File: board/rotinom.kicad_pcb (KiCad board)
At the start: 2 copper layers, 109 parts, among them J1 Conn_01x04, J2 Conn_01x04, J3 Conn_01x02, J4 Styx_P4, J5 Styx_P5, P1 test_connector, Q1 MMBT2369, Q10 MMBT2369, Q11 MMBT2369, Q12 MMBT2369, Q13 MMBT2369, Q14 MMBT2369, Q15 MMBT2369, Q16 MMBT2369, Q17 MMBT2369, Q18 MMBT2369, Q19 MMBT2369, Q2 MMBT2369, Q20 MMBT2369, Q21 MMBT2369, Q22 MMBT2369, Q23 MMBT2369, Q24 MMBT2369, Q25 MMBT2369, Q26 MMBT2369, Q27 MMBT2369, Q28 MMBT2369, Q29 MMBT2369, Q3 MMBT2369, Q30 MMBT2369, Q31 MMBT2369, Q32 MMBT2369, Q33 MMBT2369, Q4 MMBT2369, Q5 MMBT2369, Q6 MMBT2369, Q7 MMBT2369, Q8 MMBT2369, Q9 MMBT2369

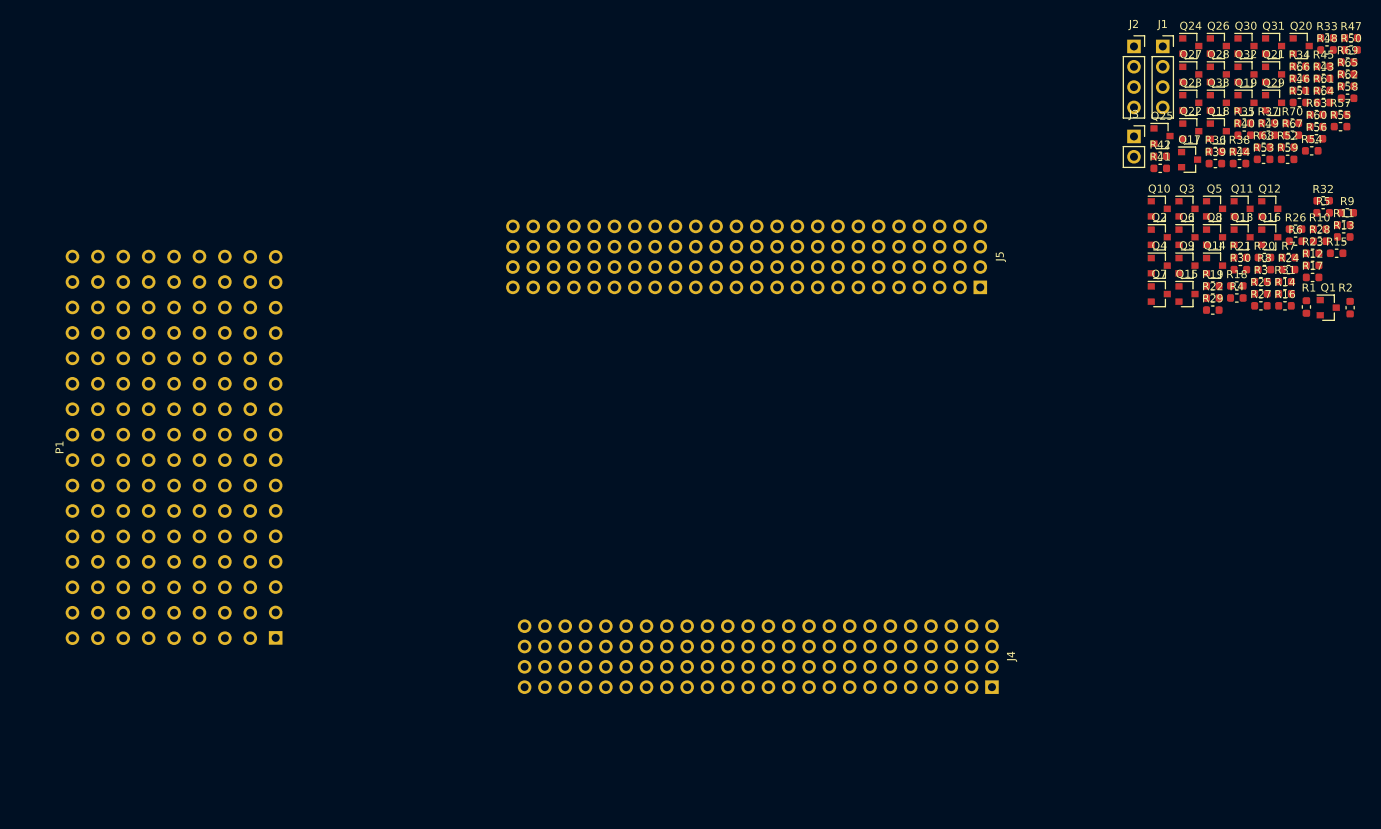
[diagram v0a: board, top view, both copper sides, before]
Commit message: Board: 5/8 of the data lanes routed
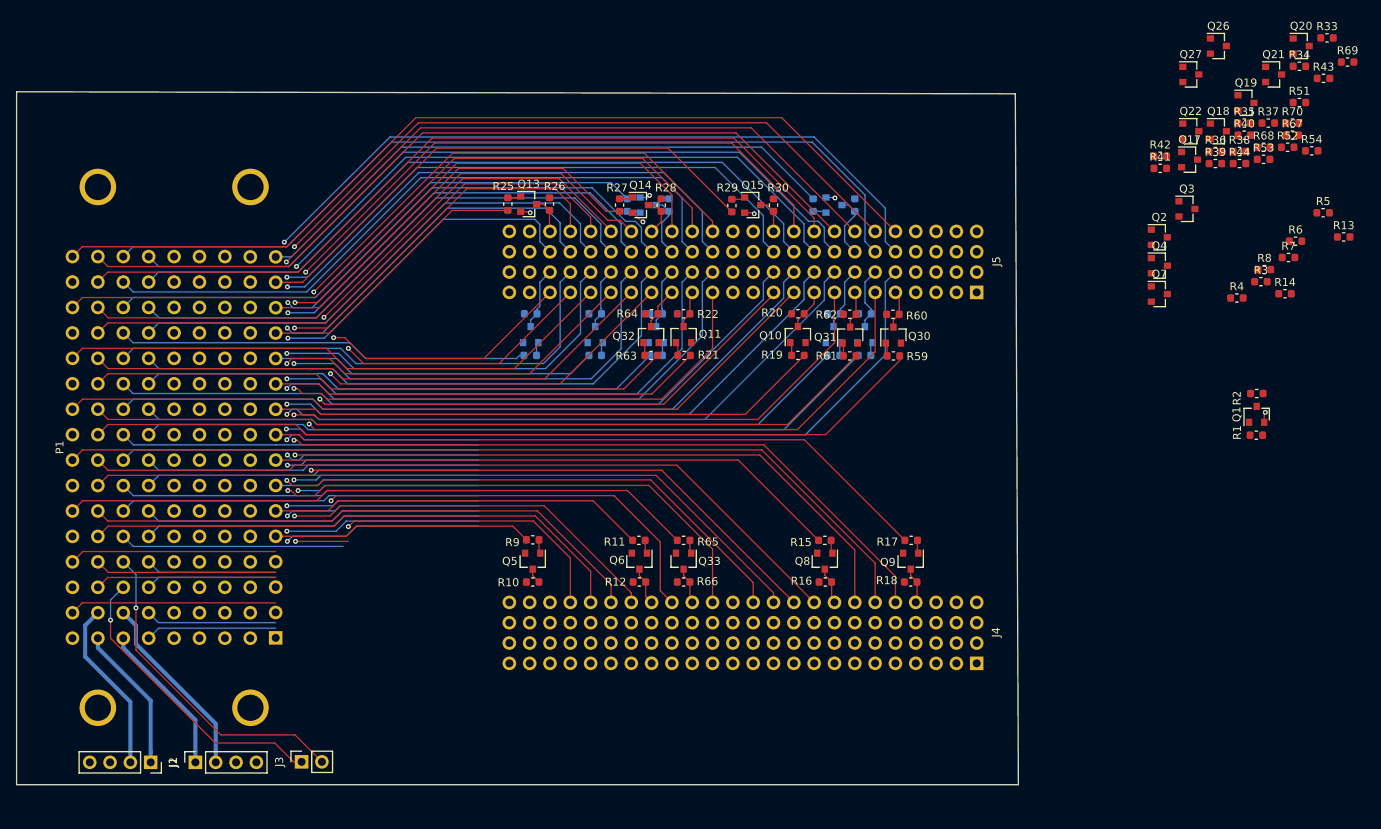
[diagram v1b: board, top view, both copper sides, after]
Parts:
- added H1: MountingHole_Pad, agc_monitor:MountingHole_ANSI_4, F.Cu at (66.7, 69.0)
- added H2: MountingHole_Pad, agc_monitor:MountingHole_ANSI_4, F.Cu at (85.8, 69.0)
- added H3: MountingHole_Pad, agc_monitor:MountingHole_ANSI_4, F.Cu at (66.7, 134.2)
- added H4: MountingHole_Pad, agc_monitor:MountingHole_ANSI_4, F.Cu at (85.8, 134.2)
- Q12, Q16, Q23, Q24, Q25, Q28, Q29, R23, R24, R31, R32, R45, R46, R47, R48, R49, R50, R55, R56, R57, R58: moved to B.Cu
- moved J1 155.0 mm to (73.3, 141.0), turned to 270 degrees
- moved J2 147.6 mm to (78.9, 141.0), turned to 90 degrees
- moved J3 130.1 mm to (92.1, 140.9), turned to 90 degrees
- moved R9 109.7 mm to (121.0, 113.2), turned to 180 degrees
- moved R10 107.8 mm to (121.0, 118.4)
- moved R55 105.3 mm to (120.7, 90.1), turned to 180 degrees
- moved R65 101.4 mm to (139.9, 113.2), turned to 180 degrees
- moved R56 100.6 mm to (120.8, 84.9)
- moved R66 99.4 mm to (139.9, 118.4)
- moved R11 96.5 mm to (134.3, 113.2), turned to 180 degrees
- moved Q5 95.9 mm to (121.0, 115.8), turned to 270 degrees
- moved R25 94.8 mm to (117.9, 71.2), turned to 270 degrees
- moved R26 93.3 mm to (123.1, 71.2), turned to 270 degrees
- moved R12 93.0 mm to (134.4, 118.4)
- moved R50 92.9 mm to (136.5, 84.9)
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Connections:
- J4 pad 16: Net-(J4-Pad16) -> MDT09_n
- J4 pad 20: Net-(J4-Pad20) -> MT09
- J4 pad 24: Net-(J4-Pad24) -> MSP908
- J4 pad 28: Net-(J4-Pad28) -> MT08
- J4 pad 32: Net-(J4-Pad32) -> MDT08_n
- J4 pad 36: Net-(J4-Pad36) -> MSCDBL_n
- J4 pad 40: Net-(J4-Pad40) -> MWL08
- J4 pad 44: Net-(J4-Pad44) -> MSP807
- J4 pad 48: Net-(J4-Pad48) -> MWL07
- J4 pad 56: Net-(J4-Pad56) -> MT07
- J4 pad 60: Net-(J4-Pad60) -> MAMU_n
- J4 pad 64: Net-(J4-Pad64) -> MT06
- J4 pad 68: Net-(J4-Pad68) -> MDT06_n
- J4 pad 72: Net-(J4-Pad72) -> MWL06
- J4 pad 76: Net-(J4-Pad76) -> MSP806
- J4 pad 80: Net-(J4-Pad80) -> MSP805
- J4 pad 84: Net-(J4-Pad84) -> MWL05
- J4 pad 88: Net-(J4-Pad88) -> MDT05_n
- J5 pad 17: Net-(J5-Pad17) -> NHALGA_n
- J5 pad 18: Net-(J5-Pad18) -> MWBG
- J5 pad 19: Net-(J5-Pad19) -> MRLG
- J5 pad 20: Net-(J5-Pad20) -> MSP916
- J5 pad 21: Net-(J5-Pad21) -> MWL09
- J5 pad 22: Net-(J5-Pad22) -> MSBSTP_n
- J5 pad 23: Net-(J5-Pad23) -> MPIPAL_n
- J5 pad 24: Net-(J5-Pad24) -> MWBBEG
- J5 pad 25: Net-(J5-Pad25) -> DOSCAL_n
- J5 pad 26: Net-(J5-Pad26) -> MRDCH_n
- J5 pad 27: Net-(J5-Pad27) -> MDT16_n
- J5 pad 28: Net-(J5-Pad28) -> MWL16
- J5 pad 29: Net-(J5-Pad29) -> MWL10
- J5 pad 30: Net-(J5-Pad30) -> MSQ10
- J5 pad 31: Net-(J5-Pad31) -> MRAG
- J5 pad 32: Net-(J5-Pad32) -> MVFAIL_n
- J5 pad 33: Net-(J5-Pad33) -> MDT10_n
- J5 pad 34: Net-(J5-Pad34) -> MGOJAM
- J5 pad 35: Net-(J5-Pad35) -> MSQ16
- J5 pad 36: Net-(J5-Pad36) -> MOSCAL_n
- J5 pad 37: Net-(J5-Pad37) -> MSP910
- J5 pad 38: Net-(J5-Pad38) -> MNISQ
- J5 pad 39: Net-(J5-Pad39) -> MWAG
- J5 pad 40: Net-(J5-Pad40) -> MWL15
- J5 pad 41: Net-(J5-Pad41) -> MT10
- J5 pad 42: Net-(J5-Pad42) -> MREQIN
- J5 pad 43: Net-(J5-Pad43) -> MSQEXT
- J5 pad 44: Net-(J5-Pad44) -> MDT15_n
- J5 pad 53: Net-(J5-Pad53) -> MT11
- J5 pad 54: Net-(J5-Pad54) -> MINHL
- J5 pad 55: Net-(J5-Pad55) -> MRSC
- J5 pad 56: Net-(J5-Pad56) -> MWEBG
- J5 pad 57: Net-(J5-Pad57) -> MDT11_n
- J5 pad 58: Net-(J5-Pad58) -> MSQ11
- J5 pad 59: Net-(J5-Pad59) -> MON800
- J5 pad 60: Net-(J5-Pad60) -> MSP914
- J5 pad 61: Net-(J5-Pad61) -> DBLTST_n
- J5 pad 62: Net-(J5-Pad62) -> MLDCH_n
- J5 pad 63: Net-(J5-Pad63) -> MREAD_n
- J5 pad 64: Net-(J5-Pad64) -> MWFBG
- J5 pad 65: Net-(J5-Pad65) -> MWL11
- J5 pad 66: Net-(J5-Pad66) -> MGP_n
- J5 pad 67: Net-(J5-Pad67) -> MONWT
- J5 pad 68: Net-(J5-Pad68) -> MDT14_n
- J5 pad 69: Net-(J5-Pad69) -> MWARNF_n
- J5 pad 70: Net-(J5-Pad70) -> MSQ12
- J5 pad 71: Net-(J5-Pad71) -> MSQ14
- J5 pad 72: Net-(J5-Pad72) -> MSCAFL_n
- J5 pad 73: Net-(J5-Pad73) -> MWL12
- J5 pad 74: Net-(J5-Pad74) -> MDT12_n
- J5 pad 75: Net-(J5-Pad75) -> MRGG
- J5 pad 76: Net-(J5-Pad76) -> MWL14
- J5 pad 77: Net-(J5-Pad77) -> MSP912
- J5 pad 78: Net-(J5-Pad78) -> MINKL
- J5 pad 79: Net-(J5-Pad79) -> MSP
- J5 pad 80: Net-(J5-Pad80) -> OUTCOM
- J5 pad 81: Net-(J5-Pad81) -> MT12
- J5 pad 82: Net-(J5-Pad82) -> MWATCH_n
- J5 pad 83: Net-(J5-Pad83) -> MSQ13
- J5 pad 84: Net-(J5-Pad84) -> MWL13
- J5 pad 85: Net-(J5-Pad85) -> MRULOG
- J5 pad 86: Net-(J5-Pad86) -> MLOAD_n
- J5 pad 87: Net-(J5-Pad87) -> MWLG
- J5 pad 88: Net-(J5-Pad88) -> MDT13_n
- R45 pad 2: MSTBSTP -> MSBSTP
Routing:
- net MSP916: track 0.00 -> 115.9 mm
- net MSP908: track 0.00 -> 111.6 mm
- net MPIPAL_n: track 0.00 -> 109.0 mm
- net NHALGA: track 0.00 -> 105.7 mm
- net MRLG: track 0.00 -> 104.7 mm, vias 0 -> 1
- net MVFAIL_n: track 0.00 -> 104.6 mm
- net MOSCAL_n: track 0.00 -> 102.8 mm
- net MWBG: track 0.00 -> 101.8 mm, vias 0 -> 1
- net DOSCAL: track 0.00 -> 99.1 mm
- net MRAG: track 0.00 -> 98.3 mm
- net MSCDBL_n: track 0.00 -> 97.4 mm
- net MSP910: track 0.00 -> 97.3 mm
- net MT09: track 0.00 -> 94.9 mm, vias 0 -> 1
- net MWBBEG: track 0.00 -> 93.8 mm, vias 0 -> 1
- net MSBSTP: track 0.00 -> 93.3 mm
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- added copper zone on In2.Cu, net GND
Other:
- board outline added: 125.2 x 86.6 mm
- copper layers 2 -> 4
- net class Default: clearance 0.2 -> 0.1524; trace_width 0.25 -> 0.1524; via_dia 0.8 -> 0.6096; via_drill 0.4 -> 0.3048
- rule trace_clearance: 0.2 -> 0.1524
- rule trace_min: 0.2 -> 0.1524
- rule via_min_drill: 0.3 -> 0.3048
- rule via_min_size: 0.4 -> 0.6096

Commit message: Board: Finished routing AGC signals; still need to route 3v3 and ground to RTL circuits
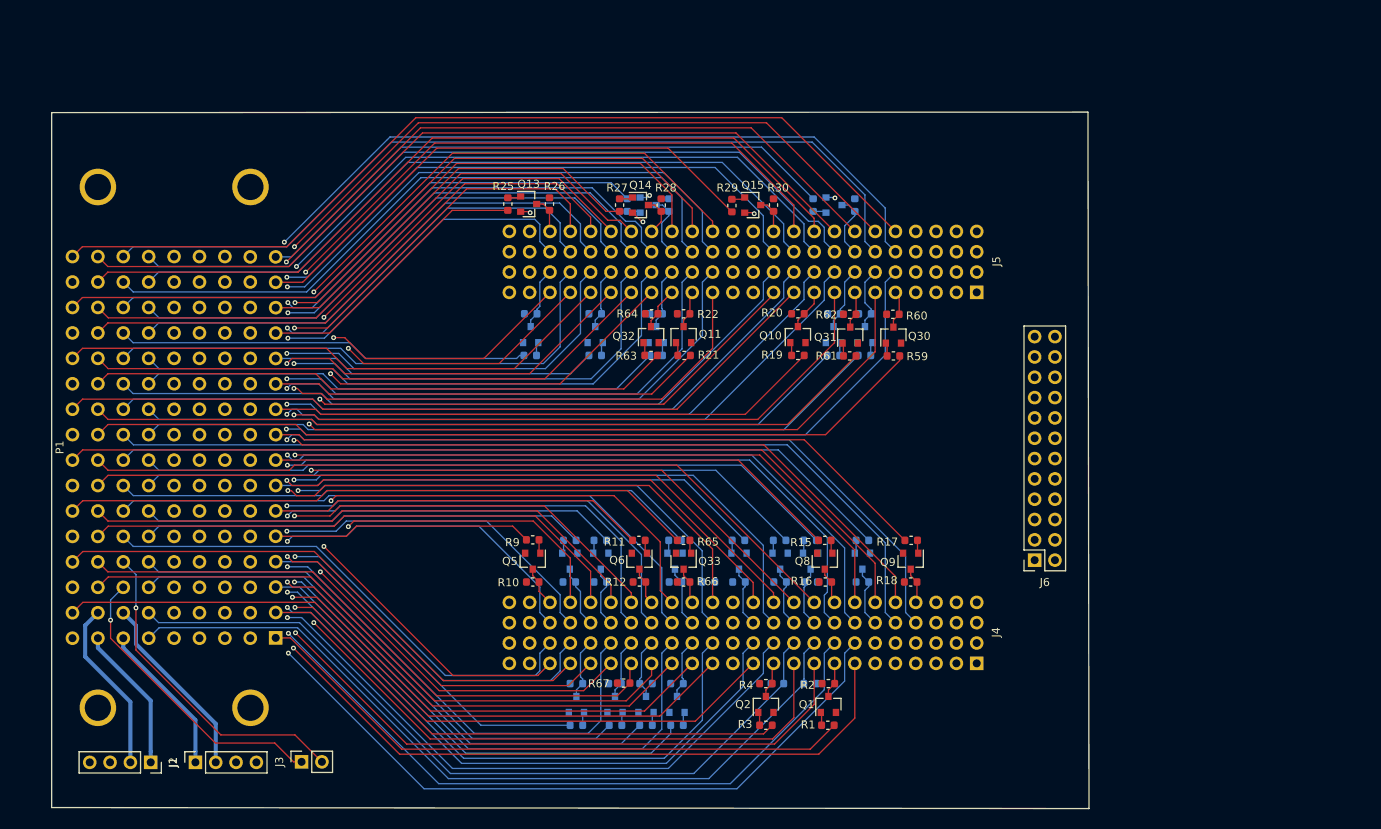
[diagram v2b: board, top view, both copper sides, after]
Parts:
- added J6: Conn_02x12_Odd_Even, Connector_PinSocket_2.54mm:PinSocket_2x12_P2.54mm_Vertical, F.Cu at (183.8, 115.7)
- Q17, Q18, Q19, Q20, Q21, Q22, Q26, Q27, Q3, Q4, Q7, R13, R14, R33, R34, R35, R36, R37, R38, R39, R40, R41, R42, R43, R44, R5, R51, R52, R53, R54, R6, R68, R69, R7, R70, R8: moved to B.Cu
- moved R33 121.0 mm to (135.2, 136.3), turned to 180 degrees
- moved R34 112.4 mm to (135.2, 131.1), turned to 180 degrees
- moved R35 108.8 mm to (131.4, 136.3), turned to 180 degrees
- moved Q20 108.7 mm to (129.5, 115.8), turned to 270 degrees
- moved R67 108.1 mm to (132.4, 131.1)
- moved R7 106.5 mm to (126.5, 136.3), turned to 180 degrees
- moved Q18 104.0 mm to (131.3, 133.7), turned to 90 degrees
- moved R5 103.1 mm to (139.1, 136.3), turned to 180 degrees
- moved R69 102.7 mm to (155.7, 131.1), turned to 180 degrees
- moved Q19 102.1 mm to (125.7, 115.8), turned to 270 degrees
- moved R37 101.7 mm to (125.7, 113.2)
- moved R8 100.4 mm to (126.5, 131.1)
- moved R36 100.3 mm to (131.3, 131.1)
- moved R38 99.6 mm to (125.6, 118.4)
- moved R40 98.0 mm to (129.5, 118.4)
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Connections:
- J4 pad 10: Net-(J4-Pad10) -> /StyxConnector/DBG7
- J4 pad 11: Net-(J4-Pad11) -> /StyxConnector/DBG12
- J4 pad 12: Net-(J4-Pad12) -> /StyxConnector/DBG14
- J4 pad 13: Net-(J4-Pad13) -> /StyxConnector/DBG3
- J4 pad 14: Net-(J4-Pad14) -> /StyxConnector/DBG8
- J4 pad 15: Net-(J4-Pad15) -> MSTPIT_n
- J4 pad 17: Net-(J4-Pad17) -> /StyxConnector/DBG4
- J4 pad 18: Net-(J4-Pad18) -> /StyxConnector/DBG9
- J4 pad 19: Net-(J4-Pad19) -> MWG
- J4 pad 2: Net-(J4-Pad2) -> /StyxConnector/DBG_3V3
- J4 pad 21: Net-(J4-Pad21) -> /StyxConnector/DBG5
- J4 pad 22: Net-(J4-Pad22) -> /StyxConnector/DBG10
- J4 pad 23: Net-(J4-Pad23) -> MONWBK_n
- J4 pad 25: Net-(J4-Pad25) -> MT01
- J4 pad 26: Net-(J4-Pad26) -> MBR1
- J4 pad 27: Net-(J4-Pad27) -> MPAL_n
- J4 pad 29: Net-(J4-Pad29) -> MDT01_n
- J4 pad 30: Net-(J4-Pad30) -> MST1
- J4 pad 31: Net-(J4-Pad31) -> MWQG
- J4 pad 33: Net-(J4-Pad33) -> MWL01
- J4 pad 34: Net-(J4-Pad34) -> STRT1
- J4 pad 35: Net-(J4-Pad35) -> MSTP_n
- J4 pad 37: Net-(J4-Pad37) -> MWL02
- J4 pad 38: Net-(J4-Pad38) -> STRT2
- J4 pad 39: Net-(J4-Pad39) -> MSTRT_n
- J4 pad 41: Net-(J4-Pad41) -> MDT02_n
- J4 pad 42: Net-(J4-Pad42) -> MST2
- J4 pad 43: Net-(J4-Pad43) -> MWYG
- J4 pad 45: Net-(J4-Pad45) -> MT02
- J4 pad 46: Net-(J4-Pad46) -> MBR2
- J4 pad 47: Net-(J4-Pad47) -> MDT07_n
- J4 pad 5: Net-(J4-Pad5) -> /StyxConnector/DBG1
- J4 pad 53: Net-(J4-Pad53) -> MSP902
- J4 pad 54: Net-(J4-Pad54) -> MIIP
- J4 pad 55: Net-(J4-Pad55) -> ALGA
- J4 pad 57: Net-(J4-Pad57) -> MT03
- J4 pad 58: Net-(J4-Pad58) -> MDT03_n
- J4 pad 59: Net-(J4-Pad59) -> MONPAR_n
- J4 pad 6: Net-(J4-Pad6) -> /StyxConnector/DBG6
- J4 pad 61: Net-(J4-Pad61) -> MWL03
- J4 pad 62: Net-(J4-Pad62) -> MST3
- J4 pad 63: Net-(J4-Pad63) -> MRCH
- J4 pad 65: Net-(J4-Pad65) -> MSP803
- J4 pad 66: Net-(J4-Pad66) -> MNHSBF_n
- J4 pad 67: Net-(J4-Pad67) -> MRPTAL_n
- J4 pad 69: Net-(J4-Pad69) -> SIGNY
- J4 pad 7: Net-(J4-Pad7) -> /StyxConnector/DBG11
- J4 pad 70: Net-(J4-Pad70) -> MNHNC_n
- J4 pad 71: Net-(J4-Pad71) -> MWZG
- J4 pad 73: Net-(J4-Pad73) -> MWL04
- J4 pad 74: Net-(J4-Pad74) -> MTCSA_n
- J4 pad 75: Net-(J4-Pad75) -> MTCSAI_n
- J4 pad 77: Net-(J4-Pad77) -> MT04
- J4 pad 78: Net-(J4-Pad78) -> MDT04_n
- J4 pad 79: Net-(J4-Pad79) -> MNHRPT_n
- J4 pad 8: Net-(J4-Pad8) -> /StyxConnector/DBG13
- J4 pad 81: Net-(J4-Pad81) -> MSP904
- J4 pad 82: Net-(J4-Pad82) -> MCTRAL_n
- J4 pad 83: Net-(J4-Pad83) -> MWSG
- J4 pad 85: Net-(J4-Pad85) -> MT05
- J4 pad 86: Net-(J4-Pad86) -> MWCH
- J4 pad 87: Net-(J4-Pad87) -> MTCAL_n
- J4 pad 9: Net-(J4-Pad9) -> /StyxConnector/DBG2
- J5 pad 11: Net-(J5-Pad11) -> /StyxConnector/DBG16
- J5 pad 12: Net-(J5-Pad12) -> /StyxConnector/DBG19
- J5 pad 15: Net-(J5-Pad15) -> /StyxConnector/DBG17
- J5 pad 16: Net-(J5-Pad16) -> /StyxConnector/DBG20
- J5 pad 7: Net-(J5-Pad7) -> /StyxConnector/DBG15
- J5 pad 8: Net-(J5-Pad8) -> /StyxConnector/DBG18
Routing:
- net MT01: track 0.00 -> 93.5 mm, vias 0 -> 1
- net MBR1: track 13.1 -> 102.5 mm, vias 0 -> 1
- net MST1: track 10.0 -> 97.9 mm, vias 0 -> 1
- net STRT1: track 16.4 -> 100.8 mm
- net STRT2: track 16.4 -> 98.0 mm
- net MWL02: track 3.69 -> 82.4 mm, vias 0 -> 1
- net MST2: track 10.0 -> 88.3 mm, vias 0 -> 1
- net MWL01: track 7.38 -> 84.2 mm, vias 0 -> 1
- net MDT01: track 0.00 -> 76.8 mm
- net MBR2: track 13.2 -> 89.9 mm, vias 0 -> 1
- net MIIP: track 13.2 -> 87.6 mm, vias 0 -> 1
- net MST3: track 10.0 -> 79.5 mm, vias 0 -> 1
- net MT02: track 6.86 -> 75.7 mm, vias 0 -> 1
- net MDT02: track 0.00 -> 68.8 mm
- net MSTPIT_n: track 39.4 -> 107.6 mm
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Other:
- board size 125.2 x 86.6 mm -> 129.7 x 87.1 mm

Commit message: Board: Basic layout done, but need to make the board longer to avoid mechanical conflict with the monitor
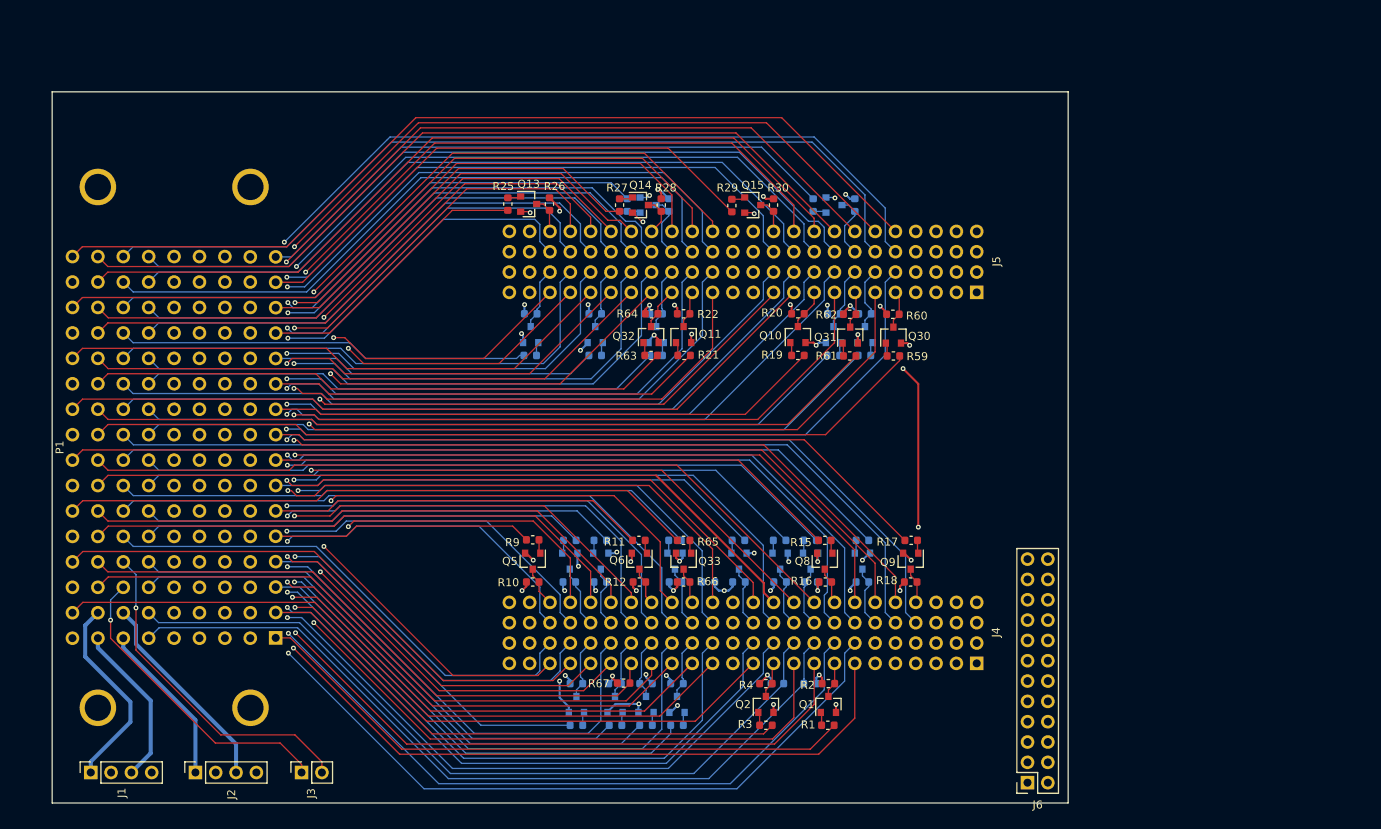
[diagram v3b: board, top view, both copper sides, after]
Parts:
- moved J6 27.8 mm to (182.9, 143.5)
- moved J1 7.60 mm to (65.8, 142.2), turned to 90 degrees
- moved J3 1.33 mm to (92.1, 142.2)
- moved J2 1.27 mm to (78.9, 142.2)
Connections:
- J1 pad 1: BPLSSW -> +4SW
- J1 pad 2: +4SW -> GND
- J1 pad 3: GND -> BPLSSW
- J2 pad 2: CTRL2 -> GND
- J2 pad 3: GND -> CTRL2
- J4 pad 11: /StyxConnector/DBG12 -> /StyxConnector/DBG10
- J4 pad 12: /StyxConnector/DBG14 -> /StyxConnector/DBG12
- J4 pad 13: /StyxConnector/DBG3 -> /StyxConnector/DBG1
- J4 pad 14: /StyxConnector/DBG8 -> /StyxConnector/DBG5
- J4 pad 17: /StyxConnector/DBG4 -> /StyxConnector/DBG2
- J4 pad 18: /StyxConnector/DBG9 -> /StyxConnector/DBG11
- J4 pad 21: /StyxConnector/DBG5 -> /StyxConnector/DBG14
- J4 pad 22: /StyxConnector/DBG10 -> /StyxConnector/DBG13
- J4 pad 5: /StyxConnector/DBG1 -> /StyxConnector/DBG3
- J4 pad 7: /StyxConnector/DBG11 -> /StyxConnector/DBG8
- J4 pad 8: /StyxConnector/DBG13 -> /StyxConnector/DBG9
- J4 pad 9: /StyxConnector/DBG2 -> /StyxConnector/DBG4
- J4 pad 93: Net-(J4-Pad93) -> +3V3_FPGA
- J4 pad 94: Net-(J4-Pad94) -> +3V3_FPGA
- J4 pad 95: Net-(J4-Pad95) -> +3V3_FPGA
- J4 pad 96: Net-(J4-Pad96) -> +3V3_FPGA
- J5 pad 15: /StyxConnector/DBG17 -> /StyxConnector/DBG15
- J5 pad 16: /StyxConnector/DBG20 -> /StyxConnector/DBG18
- J5 pad 7: /StyxConnector/DBG15 -> /StyxConnector/DBG17
- J5 pad 8: /StyxConnector/DBG18 -> /StyxConnector/DBG20
- J5 pad 90: Net-(J5-Pad90) -> +3V3_FPGA
- J5 pad 92: Net-(J5-Pad92) -> +3V3_FPGA
- J6 pad 10: /StyxConnector/DBG14 -> /StyxConnector/DBG8
- J6 pad 11: /StyxConnector/DBG5 -> /StyxConnector/DBG9
- J6 pad 12: /StyxConnector/DBG15 -> /StyxConnector/DBG10
- J6 pad 13: /StyxConnector/DBG6 -> /StyxConnector/DBG11
- J6 pad 14: /StyxConnector/DBG16 -> /StyxConnector/DBG12
- J6 pad 15: /StyxConnector/DBG7 -> /StyxConnector/DBG13
- J6 pad 16: /StyxConnector/DBG17 -> /StyxConnector/DBG14
- J6 pad 17: /StyxConnector/DBG8 -> /StyxConnector/DBG15
- J6 pad 18: /StyxConnector/DBG18 -> /StyxConnector/DBG16
- J6 pad 19: /StyxConnector/DBG9 -> /StyxConnector/DBG17
- J6 pad 20: /StyxConnector/DBG19 -> /StyxConnector/DBG18
- J6 pad 21: /StyxConnector/DBG10 -> /StyxConnector/DBG19
- J6 pad 4: /StyxConnector/DBG11 -> /StyxConnector/DBG2
- J6 pad 5: /StyxConnector/DBG2 -> /StyxConnector/DBG3
- J6 pad 6: /StyxConnector/DBG12 -> /StyxConnector/DBG4
- J6 pad 7: /StyxConnector/DBG3 -> /StyxConnector/DBG5
- J6 pad 8: /StyxConnector/DBG13 -> /StyxConnector/DBG6
- J6 pad 9: /StyxConnector/DBG4 -> /StyxConnector/DBG7
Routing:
- net +3V3_FPGA: track 0.00 -> 283.5 mm, vias 0 -> 30
- net GND: track 6.73 -> 46.7 mm, vias 5 -> 27
- net +4SW: track 21.7 -> 25.0 mm
- net CTRL2: track 23.5 -> 25.8 mm
- net BPLSSW: track 18.3 -> 20.5 mm
- net MTLO: track 40.7 -> 42.0 mm
- net CTRL1: track 19.3 -> 20.5 mm
- net MTHI: track 37.3 -> 38.4 mm
- added copper zone on In1.Cu, net GND
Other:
- board size 129.7 x 87.1 mm -> 127 x 88.9 mm
